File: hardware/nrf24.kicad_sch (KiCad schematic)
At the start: 20 parts, among them U2 nRF24L01P, Y1 16MHz

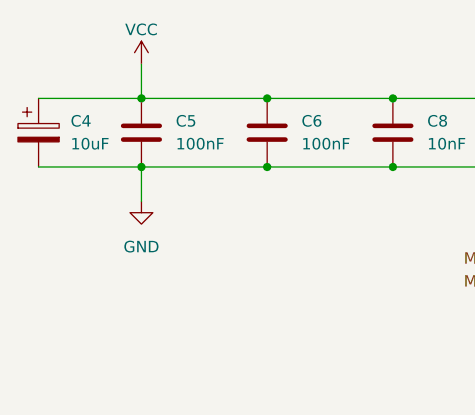
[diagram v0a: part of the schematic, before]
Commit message: Updated decoupling caps
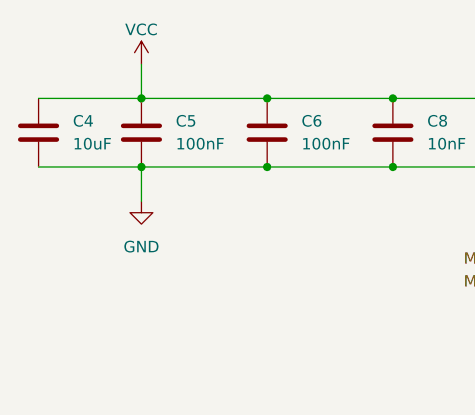
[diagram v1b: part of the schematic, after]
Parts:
- removed C4: 10uF, symbol Device:C_Polarized
- added C4: 10uF, symbol Device:C
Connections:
- net GND: now also C4.2
- net VCC: now also C4.1
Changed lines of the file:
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@@
+	)
+	(symbol
+		(lib_id "Device:C")
+		(at 60.96 73.66 0)
+		(unit 1)
+		(exclude_from_sim no)
+		(in_bom yes)
+		(on_board yes)
+		(dnp no)
+		(fields_autoplaced yes)
+		(property "Reference" "C4"
+			(at 64.77 72.3899 0)
+			(effects
+				(font
+					(size 1.27 1.27)
+				)
+				(justify left)
+			)
+		)
+		(property "Value" "10uF"
+			(at 64.77 74.9299 0)
+			(effects
+				(font
+					(size 1.27 1.27)
+				)
+				(justify left)
+			)
+		)
+		(property "Footprint" ""
+			(at 61.9252 77.47 0)
+			(effects
+				(font
+					(size 1.27 1.27)
+				)
+				(hide yes)
+			)
+		)
+		(property "Datasheet" "~"
+			(at 60.96 73.66 0)
+			(effects
+				(font
+					(size 1.27 1.27)
+				)
+				(hide yes)
+			)
+		)
+		(property "Description" "Unpolarized capacitor"
+			(at 60.96 73.66 0)
+			(effects
+				(font
+					(size 1.27 1.27)
+				)
+				(hide yes)
+			)
+		)
+		(pin "1"
+		)
+		(pin "2"
+		)
+		(instances
+			(project ""
+				(path "/c384ea46-0dfb-4673-b2f4-1f88fafbcaa5/0b31be65-dd8f-4cfe-9626-c0e264a9ba4c"
+					(reference "C4")
+					(unit 1)
+				)
+			)
+		)
 	)
 	(symbol
@@
 					(unit 1)
 				)
-			)
-		)
-	)
-	(symbol
-		(lib_id "Device:C_Polarized")
-		(at 60.96 73.66 0)
-		(unit 1)
-		(exclude_from_sim no)
-		(in_bom yes)
-		(on_board yes)
-		(dnp no)
-		(property "Reference" "C4"
-			(at 64.516 72.39 0)
-			(effects
-				(font
-					(size 1.27 1.27)
-				)
-				(justify left)
-			)
-		)
-		(property "Value" "10uF"
-			(at 64.516 74.93 0)
-			(effects
-				(font
-					(size 1.27 1.27)
-				)
-				(justify left)
-			)
-		)
-		(property "Footprint" ""
-			(at 61.9252 77.47 0)
-			(effects
-				(font
-					(size 1.27 1.27)
-				)
-				(hide yes)
-			)
-		)
-		(property "Datasheet" "~"
-			(at 60.96 73.66 0)
-			(effects
-				(font
-					(size 1.27 1.27)
-				)
-				(hide yes)
-			)
-		)
-		(property "Description" "Polarized capacitor"
-			(at 60.96 73.66 0)
-			(effects
-				(font
-					(size 1.27 1.27)
-				)
-				(hide yes)
-			)
-		)
-		(pin "1"
-		)
-		(pin "2"
-		)
-		(instances
-			(project "heli_avionics"
-				(path "/c384ea46-0dfb-4673-b2f4-1f88fafbcaa5/0b31be65-dd8f-4cfe-9626-c0e264a9ba4c"
-					(reference "C4")
-					(unit 1)
-				)

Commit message: Updated footprints for the IC's
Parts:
- U2: footprint Package_DFN_QFN:QFN-20-1EP_4x4mm_P0.5mm_EP2.5x2.5mm -> heli-footprints:NRF24L01_HandSolder_SpecialPad
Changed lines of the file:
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@@
 			)
 		)
-		(property "Footprint" "Package_DFN_QFN:QFN-20-1EP_4x4mm_P0.5mm_EP2.5x2.5mm"
+		(property "Footprint" "heli-footprints:NRF24L01_HandSolder_SpecialPad"
 			(at 138.43 80.01 0)
 			(effects

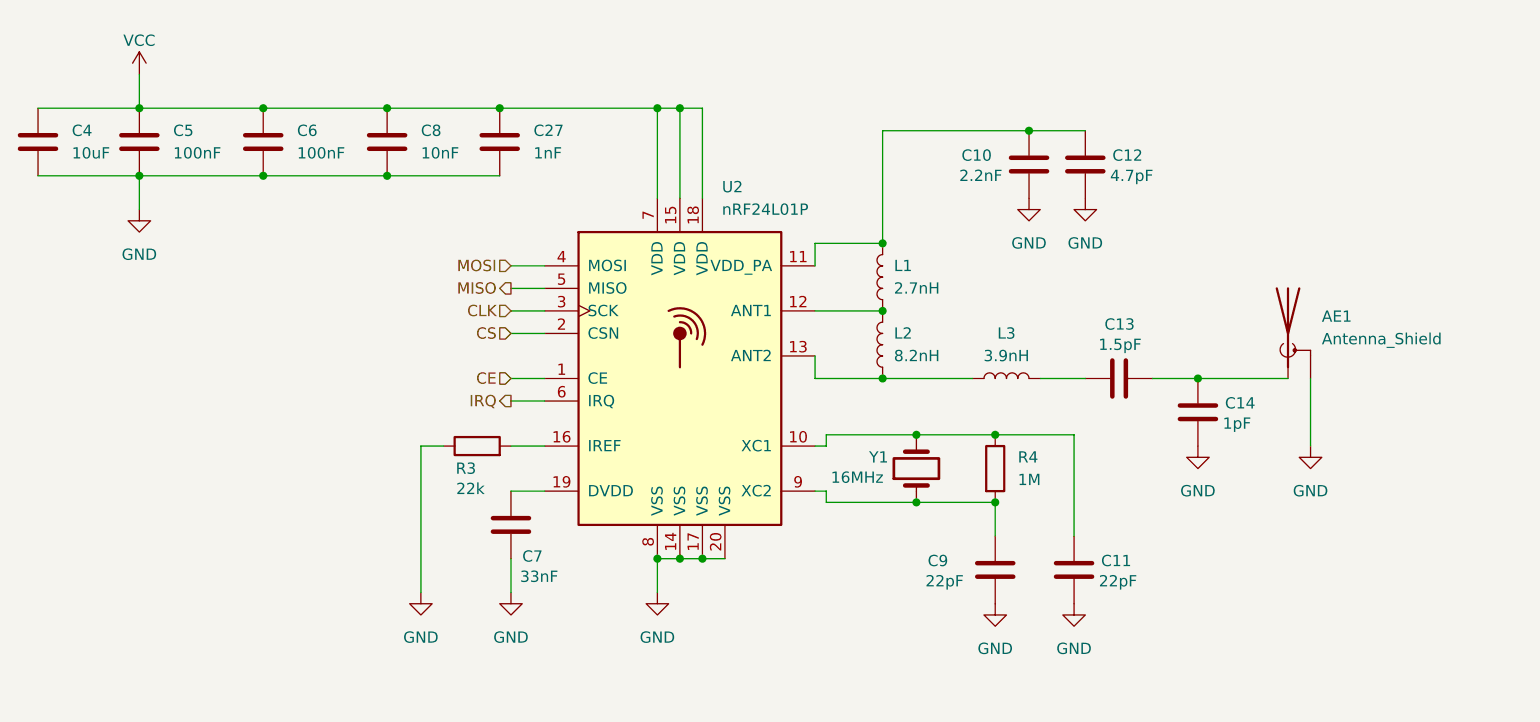
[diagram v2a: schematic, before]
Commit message: Assigned footprint for crystal and button, fixed gitignore
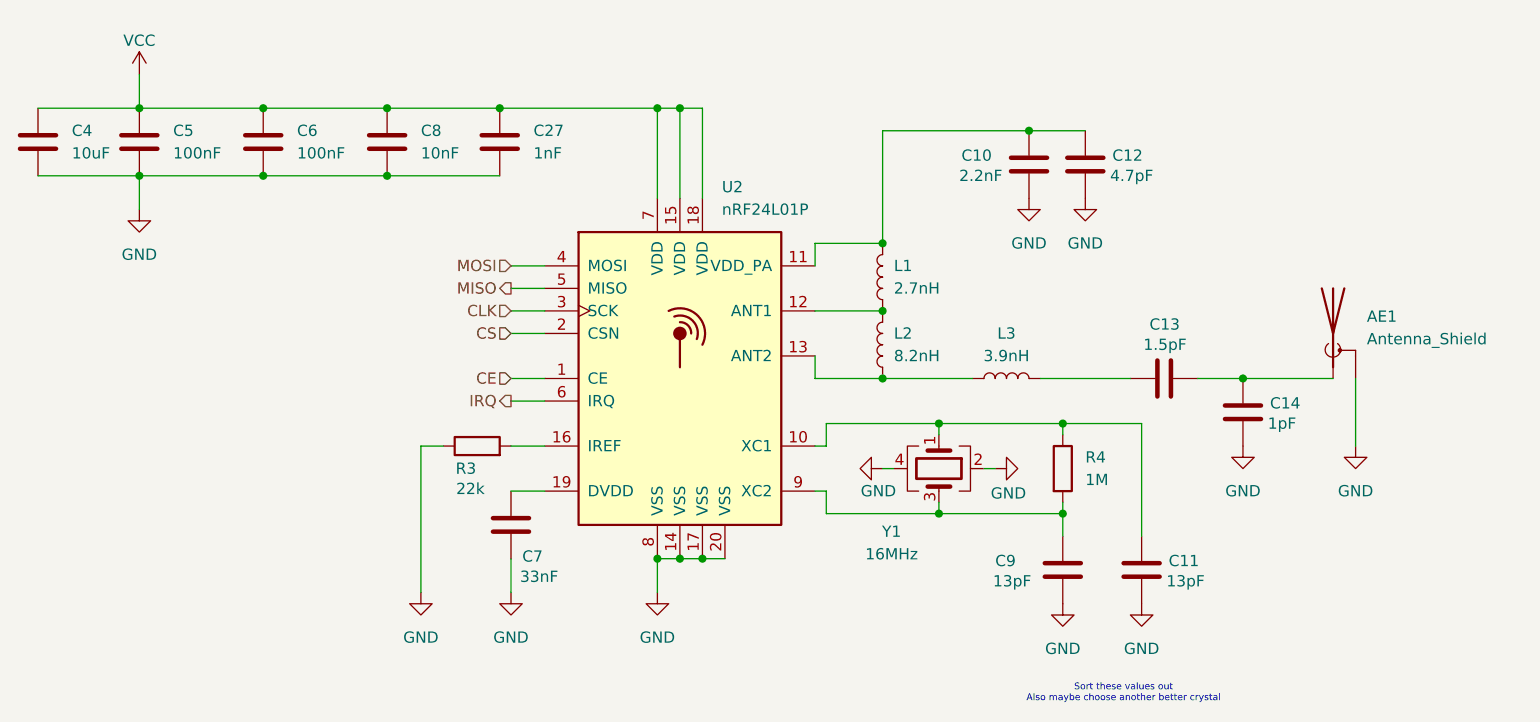
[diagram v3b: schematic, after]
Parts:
- removed Y1: 16MHz, symbol Device:Crystal
- added Y1: 16MHz, Crystal:Crystal_SMD_3225-4Pin_3.2x2.5mm, symbol Device:Crystal_GND24
- C11, C9: value 22pF -> 13pF
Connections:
- net GND: now also Y1.2, Y1.4
- net at C9.1, R4.2, U2.9 (XC2): now also Y1.3
- net at C11.1, R4.1, U2.10 (XC1): now also Y1.1
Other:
- note added: "Sort these values out Also maybe choose another better crystal"
- moved on the sheet: AE1, C11, C13, C14, C9, R4

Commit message: Assigned footprints for capacitors and inductors
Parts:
- AE1: footprint (none) -> Connector_Wire:SolderWire-0.5sqmm_1x01_D0.9mm_OD2.1mm
- C10, C11, C12, C13, C14, C27, C4, C5, C6, C7, C8, C9: footprint (none) -> Capacitor_SMD:C_0603_1608Metric_Pad1.08x0.95mm_HandSolder
- L1, L2, L3: footprint (none) -> Inductor_SMD:L_0603_1608Metric_Pad1.05x0.95mm_HandSolder
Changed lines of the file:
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@@
 			)
 		)
-		(property "Footprint" ""
+		(property "Footprint" "Capacitor_SMD:C_0603_1608Metric_Pad1.08x0.95mm_HandSolder"
 			(at 73.3552 77.47 0)
 			(effects
@@
 			)
 		)
-		(property "Footprint" ""
+		(property "Footprint" "Capacitor_SMD:C_0603_1608Metric_Pad1.08x0.95mm_HandSolder"
 			(at 87.3252 77.47 0)
 			(effects
@@
 			)
 		)
-		(property "Footprint" ""
+		(property "Footprint" "Capacitor_SMD:C_0603_1608Metric_Pad1.08x0.95mm_HandSolder"
 			(at 101.2952 77.47 0)
 			(effects
@@
 			)
 		)
-		(property "Footprint" ""
+		(property "Footprint" "Capacitor_SMD:C_0603_1608Metric_Pad1.08x0.95mm_HandSolder"
 			(at 197.8152 107.95 0)
 			(effects
@@
 			)
 		)
-		(property "Footprint" ""
+		(property "Footprint" "Connector_Wire:SolderWire-0.5sqmm_1x01_D0.9mm_OD2.1mm"
 			(at 207.01 92.71 0)
 			(effects
@@
 			)
 		)
-		(property "Footprint" ""
+		(property "Footprint" "Capacitor_SMD:C_0603_1608Metric_Pad1.08x0.95mm_HandSolder"
 			(at 191.77 99.3648 0)
 			(effects
@@
 			)
 		)
-		(property "Footprint" ""
+		(property "Footprint" "Capacitor_SMD:C_0603_1608Metric_Pad1.08x0.95mm_HandSolder"
 			(at 61.9252 77.47 0)
 			(effects
@@
 			)
 		)
-		(property "Footprint" ""
+		(property "Footprint" "Inductor_SMD:L_0603_1608Metric_Pad1.05x0.95mm_HandSolder"
 			(at 156.21 88.9 0)
 			(effects
@@
 			)
 		)
-		(property "Footprint" ""
+		(property "Footprint" "Capacitor_SMD:C_0603_1608Metric_Pad1.08x0.95mm_HandSolder"
 			(at 180.0352 80.01 0)
 			(effects
@@
 			)
 		)
-		(property "Footprint" ""
+		(property "Footprint" "Inductor_SMD:L_0603_1608Metric_Pad1.05x0.95mm_HandSolder"
 			(at 170.18 100.33 0)
 			(effects
@@
 			)
 		)
-		(property "Footprint" ""
+		(property "Footprint" "Capacitor_SMD:C_0603_1608Metric_Pad1.08x0.95mm_HandSolder"
 			(at 186.3852 125.73 0)
 			(effects
@@
 			)
 		)
-		(property "Footprint" ""
+		(property "Footprint" "Capacitor_SMD:C_0603_1608Metric_Pad1.08x0.95mm_HandSolder"
 			(at 173.6852 80.01 0)
 			(effects
@@
 			)
 		)
-		(property "Footprint" ""
+		(property "Footprint" "Capacitor_SMD:C_0603_1608Metric_Pad1.08x0.95mm_HandSolder"
 			(at 177.4952 125.73 0)
 			(effects
@@
 			)
 		)
-		(property "Footprint" ""
+		(property "Footprint" "Inductor_SMD:L_0603_1608Metric_Pad1.05x0.95mm_HandSolder"
 			(at 156.21 96.52 0)
 			(effects
@@
 			)
 		)
-		(property "Footprint" ""
+		(property "Footprint" "Capacitor_SMD:C_0603_1608Metric_Pad1.08x0.95mm_HandSolder"
 			(at 115.2652 120.65 0)
 			(effects
@@
 			)
 		)
-		(property "Footprint" ""
+		(property "Footprint" "Capacitor_SMD:C_0603_1608Metric_Pad1.08x0.95mm_HandSolder"
 			(at 113.9952 77.47 0)
 			(effects

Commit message: Assigned resistor footprints
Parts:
- R3, R4: footprint (none) -> Resistor_SMD:R_0603_1608Metric_Pad0.98x0.95mm_HandSolder
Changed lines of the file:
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@@
 			)
 		)
-		(property "Footprint" ""
+		(property "Footprint" "Resistor_SMD:R_0603_1608Metric_Pad0.98x0.95mm_HandSolder"
 			(at 110.49 109.728 90)
 			(effects
@@
 			)
 		)
-		(property "Footprint" ""
+		(property "Footprint" "Resistor_SMD:R_0603_1608Metric_Pad0.98x0.95mm_HandSolder"
 			(at 174.752 110.49 90)
 			(effects

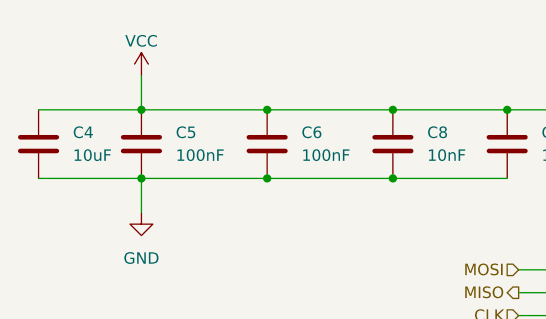
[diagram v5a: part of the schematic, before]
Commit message: Added separate LDO for NRF24
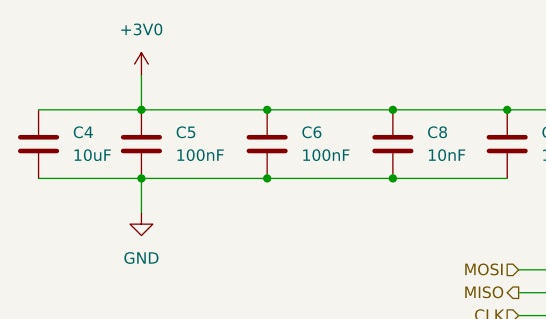
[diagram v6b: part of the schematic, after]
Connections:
- net VCC renamed +3V0
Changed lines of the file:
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@@
+	)
+	(symbol
+		(lib_id "power:+3V0")
+		(at 72.39 66.04 0)
+		(unit 1)
+		(exclude_from_sim no)
+		(in_bom yes)
+		(on_board yes)
+		(dnp no)
+		(fields_autoplaced yes)
+		(property "Reference" "#PWR010"
+			(at 72.39 69.85 0)
+			(effects
+				(font
+					(size 1.27 1.27)
+				)
+				(hide yes)
+			)
+		)
+		(property "Value" "+3V0"
+			(at 72.39 60.96 0)
+			(effects
+				(font
+					(size 1.27 1.27)
+				)
+			)
+		)
+		(property "Footprint" ""
+			(at 72.39 66.04 0)
+			(effects
+				(font
+					(size 1.27 1.27)
+				)
+				(hide yes)
+			)
+		)
+		(property "Datasheet" ""
+			(at 72.39 66.04 0)
+			(effects
+				(font
+					(size 1.27 1.27)
+				)
+				(hide yes)
+			)
+		)
+		(property "Description" "Power symbol creates a global label with name \"+3V0\""
+			(at 72.39 66.04 0)
+			(effects
+				(font
+					(size 1.27 1.27)
+				)
+				(hide yes)
+			)
+		)
+		(pin "1"
+		)
+		(instances
+			(project ""
+				(path "/c384ea46-0dfb-4673-b2f4-1f88fafbcaa5/0b31be65-dd8f-4cfe-9626-c0e264a9ba4c"
+					(reference "#PWR010")
+					(unit 1)
+				)
+			)
+		)
 	)
 	(symbol
@@
 					(unit 1)
 				)
-			)
-		)
-	)
-	(symbol
-		(lib_id "power:VCC")
-		(at 72.39 66.04 0)
-		(unit 1)
-		(exclude_from_sim no)
-		(in_bom yes)
-		(on_board yes)
-		(dnp no)
-		(property "Reference" "#PWR010"
-			(at 72.39 69.85 0)
-			(effects
-				(font
-					(size 1.27 1.27)
-				)
-				(hide yes)
-			)
-		)
-		(property "Value" "VCC"
-			(at 72.39 62.23 0)
-			(effects
-				(font
-					(size 1.27 1.27)
-				)
-			)
-		)
-		(property "Footprint" ""
-			(at 72.39 66.04 0)
-			(effects
-				(font
-					(size 1.27 1.27)
-				)
-				(hide yes)
-			)
-		)
-		(property "Datasheet" ""
-			(at 72.39 66.04 0)
-			(effects
-				(font
-					(size 1.27 1.27)
-				)
-				(hide yes)
-			)
-		)
-		(property "Description" "Power symbol creates a global label with name \"VCC\""
-			(at 72.39 66.04 0)
-			(effects
-				(font
-					(size 1.27 1.27)
-				)
-				(hide yes)
-			)
-		)
-		(pin "1"
-		)
-		(instances
-			(project "heli_avionics"
-				(path "/c384ea46-0dfb-4673-b2f4-1f88fafbcaa5/0b31be65-dd8f-4cfe-9626-c0e264a9ba4c"
-					(reference "#PWR010")
-					(unit 1)
-				)

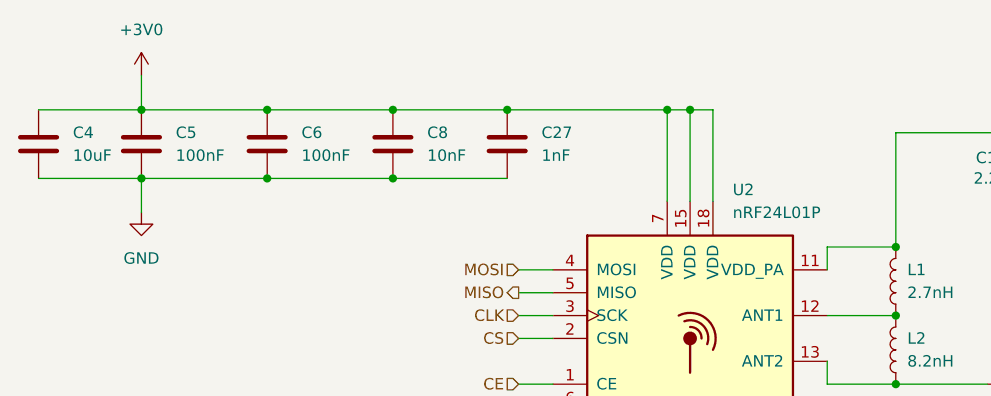
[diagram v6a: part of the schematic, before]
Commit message: Updated decoupling caps to match guidelines from Eric Bogatin
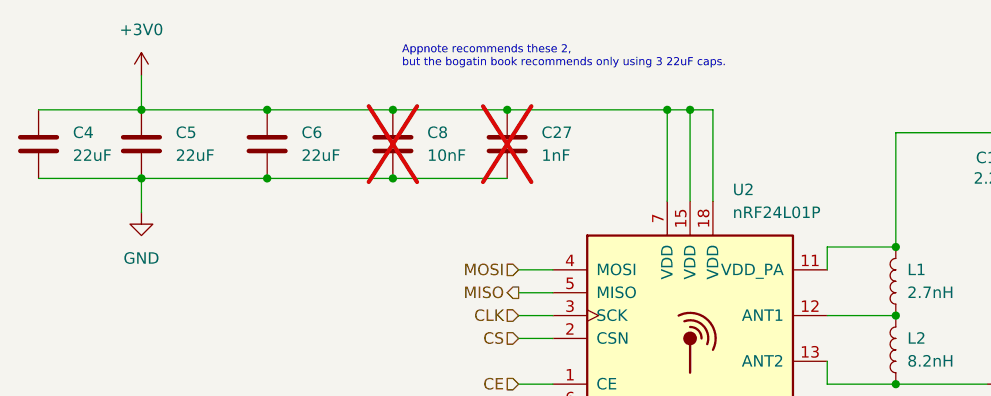
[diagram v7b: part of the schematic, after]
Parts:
- C27, C8: now not fitted
- C4: value 10uF -> 22uF
- C5, C6: value 100nF -> 22uF
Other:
- note added: "Appnote recommends these 2, but the bogatin book recommends only using 3 22uF caps."
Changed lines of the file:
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@@
+		)
+	)
+	(text "Appnote recommends these 2,\nbut the bogatin book recommends only using 3 22uF caps."
+		(exclude_from_sim no)
+		(at 101.346 64.008 0)
+		(effects
+			(font
+				(size 0.889 0.889)
+			)
+			(justify left)
 		)
 	)
@@
 			)
 		)
-		(property "Value" "100nF"
+		(property "Value" "22uF"
 			(at 76.2 74.9299 0)
 			(effects
@@
 			)
 		)
-		(property "Value" "100nF"
+		(property "Value" "22uF"
 			(at 90.17 74.9299 0)
 			(effects
@@
 		(in_bom yes)
 		(on_board yes)
-		(dnp no)
+		(dnp yes)
 		(fields_autoplaced yes)
 		(property "Reference" "C8"
@@
 			)
 		)
-		(property "Value" "10uF"
+		(property "Value" "22uF"
 			(at 64.77 74.9299 0)
 			(effects
@@
 		(in_bom yes)
 		(on_board yes)
-		(dnp no)
+		(dnp yes)
 		(fields_autoplaced yes)
 		(property "Reference" "C27"

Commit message: Layout savepoint 1
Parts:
- removed AE1: Antenna_Shield, Connector_Wire:SolderWire-0.5sqmm_1x01_D0.9mm_OD2.1mm, symbol Device:Antenna_Shield
- added AE1: Antenna, Connector_Wire:SolderWire-0.5sqmm_1x01_D0.9mm_OD2.1mm, symbol Device:Antenna
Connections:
- net at C13.2, C14.1: now also AE1.1 (A)
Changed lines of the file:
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@@
-	(wire
-		(pts
-			(xy 209.55 100.33) (xy 209.55 107.95)
-		)
-		(stroke
-			(width 0)
-			(type default)
-		)
-	)
 	(wire
 		(pts
@@
 	)
 	(symbol
+		(lib_id "Device:Antenna")
+		(at 207.01 95.25 0)
+		(unit 1)
+		(exclude_from_sim no)
+		(in_bom yes)
+		(on_board yes)
+		(dnp no)
+		(fields_autoplaced yes)
+		(property "Reference" "AE1"
+			(at 209.55 94.6149 0)
+			(effects
+				(font
+					(size 1.27 1.27)
+				)
+				(justify left)
+			)
+		)
+		(property "Value" "Antenna"
+			(at 209.55 97.1549 0)
+			(effects
+				(font
+					(size 1.27 1.27)
+				)
+				(justify left)
+			)
+		)
+		(property "Footprint" "Connector_Wire:SolderWire-0.5sqmm_1x01_D0.9mm_OD2.1mm"
+			(at 207.01 95.25 0)
+			(effects
+				(font
+					(size 1.27 1.27)
+				)
+				(hide yes)
+			)
+		)
+		(property "Datasheet" "~"
+			(at 207.01 95.25 0)
+			(effects
+				(font
+					(size 1.27 1.27)
+				)
+				(hide yes)
+			)
+		)
+		(property "Description" "Antenna"
+			(at 207.01 95.25 0)
+			(effects
+				(font
+					(size 1.27 1.27)
+				)
+				(hide yes)
+			)
+		)
+		(pin "1"
+		)
+		(instances
+			(project ""
+				(path "/c384ea46-0dfb-4673-b2f4-1f88fafbcaa5/0b31be65-dd8f-4cfe-9626-c0e264a9ba4c"
+					(reference "AE1")
+					(unit 1)
+				)
+			)
+		)
+	)
+	(symbol
 		(lib_id "power:GND")
 		(at 72.39 81.28 0)
@@
 	)
 	(symbol
-		(lib_id "Device:Antenna_Shield")
-		(at 207.01 95.25 0)
-		(unit 1)
-		(exclude_from_sim no)
-		(in_bom yes)
-		(on_board yes)
-		(dnp no)
-		(fields_autoplaced yes)
-		(property "Reference" "AE1"
-			(at 210.82 93.3449 0)
-			(effects
-				(font
-					(size 1.27 1.27)
-				)
-				(justify left)
-			)
-		)
-		(property "Value" "Antenna_Shield"
-			(at 210.82 95.8849 0)
-			(effects
-				(font
-					(size 1.27 1.27)
-				)
-				(justify left)
-			)
-		)
-		(property "Footprint" "Connector_Wire:SolderWire-0.5sqmm_1x01_D0.9mm_OD2.1mm"
-			(at 207.01 92.71 0)
-			(effects
-				(font
-					(size 1.27 1.27)
-				)
-				(hide yes)
-			)
-		)
-		(property "Datasheet" "~"
-			(at 207.01 92.71 0)
-			(effects
-				(font
-					(size 1.27 1.27)
-				)
-				(hide yes)
-			)
-		)
-		(property "Description" "Antenna with extra pin for shielding"
-			(at 207.01 95.25 0)
-			(effects
-				(font
-					(size 1.27 1.27)
-				)
-				(hide yes)
-			)
-		)
-		(pin "2"
-		)
-		(pin "1"
-		)
-		(instances
-			(project "heli_avionics"
-				(path "/c384ea46-0dfb-4673-b2f4-1f88fafbcaa5/0b31be65-dd8f-4cfe-9626-c0e264a9ba4c"
-					(reference "AE1")
-					(unit 1)
-				)
-			)
-		)
-	)
-	(symbol
 		(lib_id "power:GND")
 		(at 185.42 125.73 0)
@@
 					(unit 1)
 				)
-			)
-		)
-	)
-	(symbol
-		(lib_id "power:GND")
-		(at 209.55 107.95 0)
-		(unit 1)
-		(exclude_from_sim no)
-		(in_bom yes)
-		(on_board yes)
-		(dnp no)
-		(fields_autoplaced yes)
-		(property "Reference" "#PWR020"
-			(at 209.55 114.3 0)
-			(effects
-				(font
-					(size 1.27 1.27)
-				)
-				(hide yes)
-			)
-		)
-		(property "Value" "GND"
-			(at 209.55 113.03 0)
-			(effects
-				(font
-					(size 1.27 1.27)
-				)
-			)
-		)
-		(property "Footprint" ""
-			(at 209.55 107.95 0)
-			(effects
-				(font
-					(size 1.27 1.27)
-				)
-				(hide yes)
-			)
-		)
-		(property "Datasheet" ""
-			(at 209.55 107.95 0)
-			(effects
-				(font
-					(size 1.27 1.27)
-				)
-				(hide yes)
-			)
-		)
-		(property "Description" "Power symbol creates a global label with name \"GND\" , ground"
-			(at 209.55 107.95 0)
-			(effects
-				(font
-					(size 1.27 1.27)
-				)
-				(hide yes)
-			)
-		)
-		(pin "1"
-		)
-		(instances
-			(project "heli_avionics"
-				(path "/c384ea46-0dfb-4673-b2f4-1f88fafbcaa5/0b31be65-dd8f-4cfe-9626-c0e264a9ba4c"
-					(reference "#PWR020")
-					(unit 1)
-				)
